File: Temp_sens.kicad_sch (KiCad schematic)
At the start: 16 parts, among them J3001 PT_1000, Q3001 IRLML5103, U3001 ADA4807-1

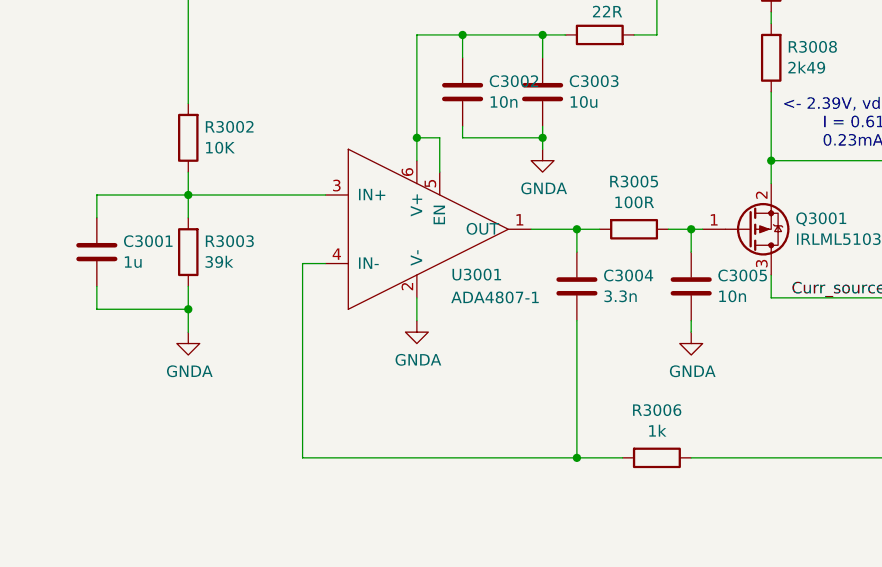
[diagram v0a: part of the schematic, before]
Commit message: added second AMUX and housekeeping
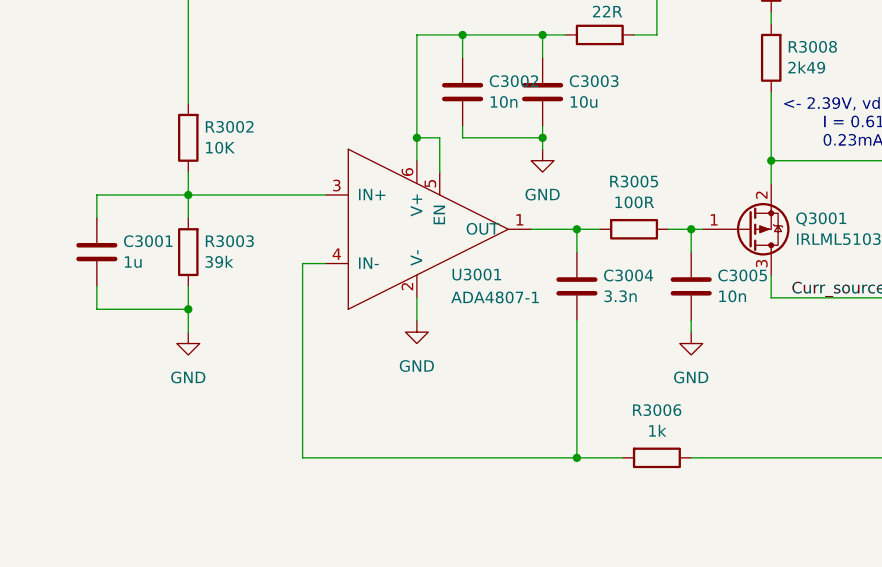
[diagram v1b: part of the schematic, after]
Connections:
- net GNDA is gone; now on net GND: C3001.2, C3002.2, C3003.2, C3005.2, R3003.1, U3001.2 (V-)

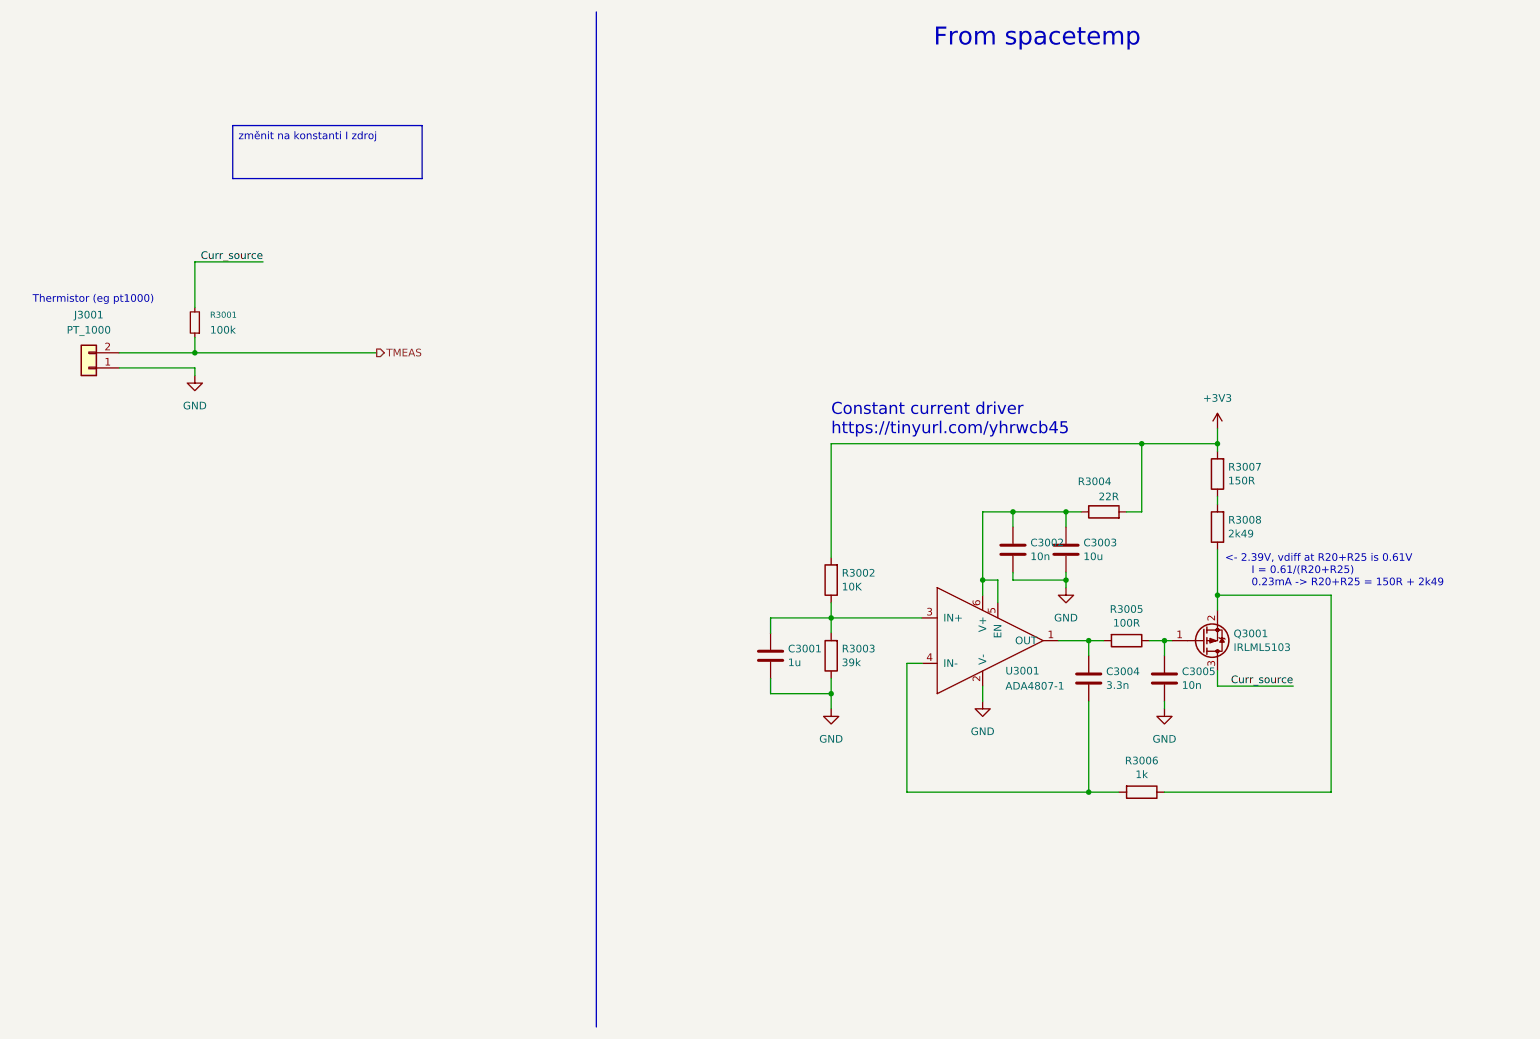
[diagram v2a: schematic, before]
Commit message: updated battery pack module; updated solar inputs module
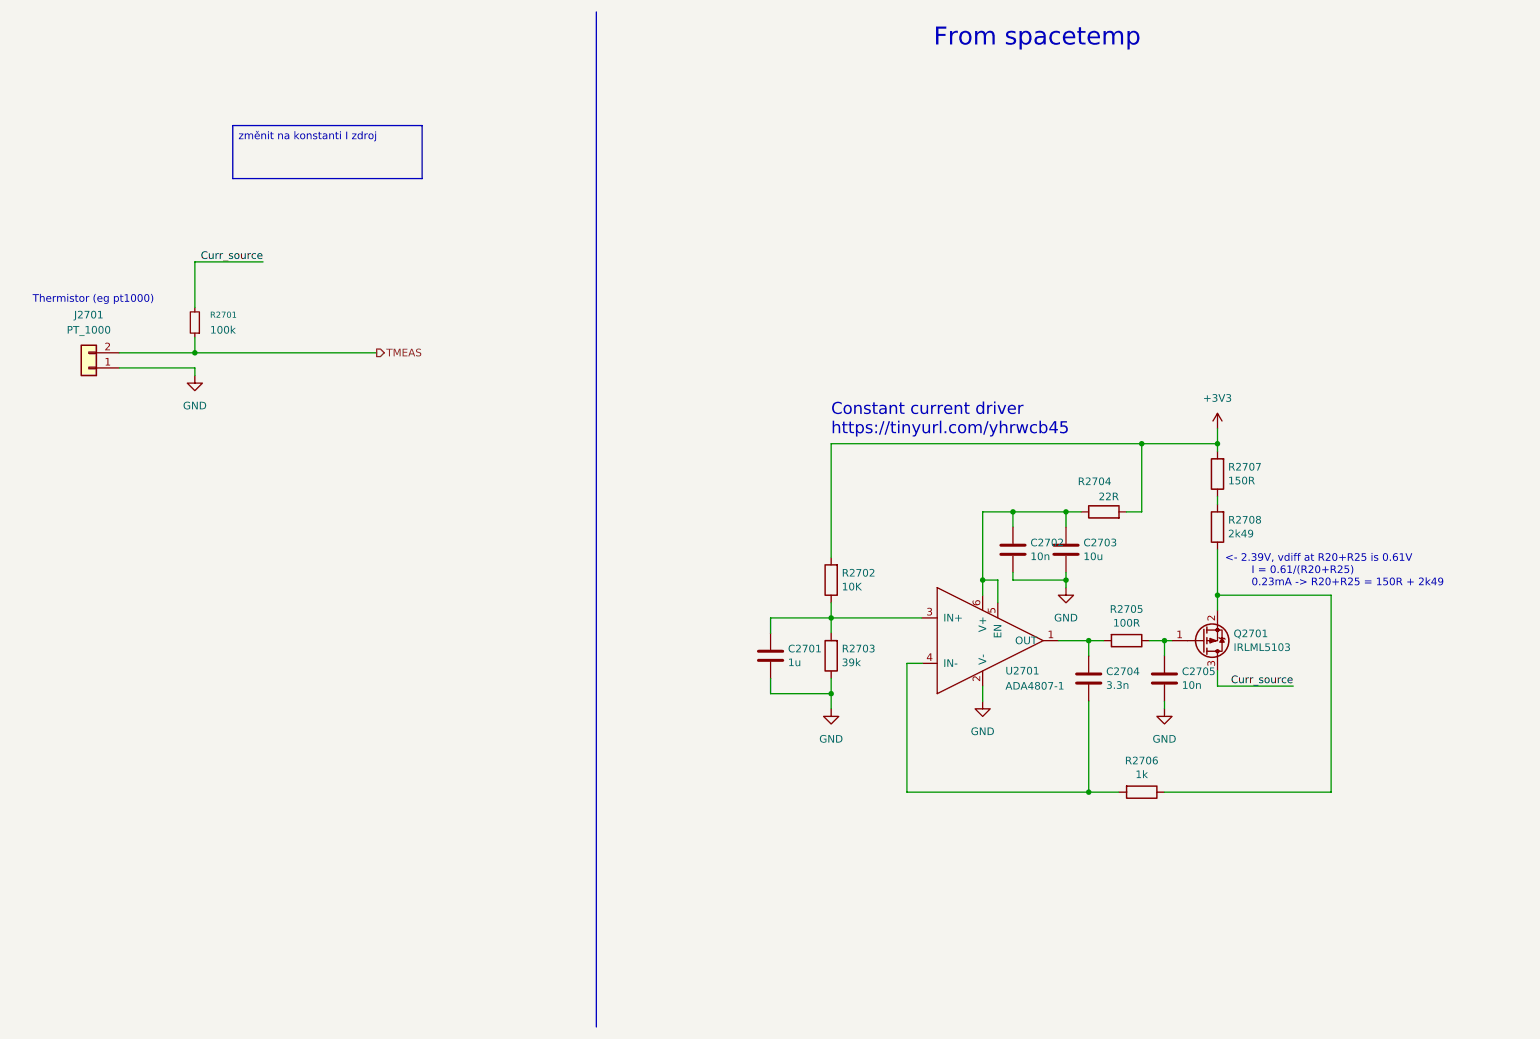
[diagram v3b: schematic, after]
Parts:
- renumbered C3001 to C2701, C3002 to C2702, C3003 to C2703, C3004 to C2704, C3005 to C2705, J3001 to J2701, Q3001 to Q2701, R3001 to R2701, R3002 to R2702, R3003 to R2703, R3004 to R2704, R3005 to R2705, R3006 to R2706, R3007 to R2707, R3008 to R2708, U3001 to U2701

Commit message: wired channel alerts; added schematic for test pbc
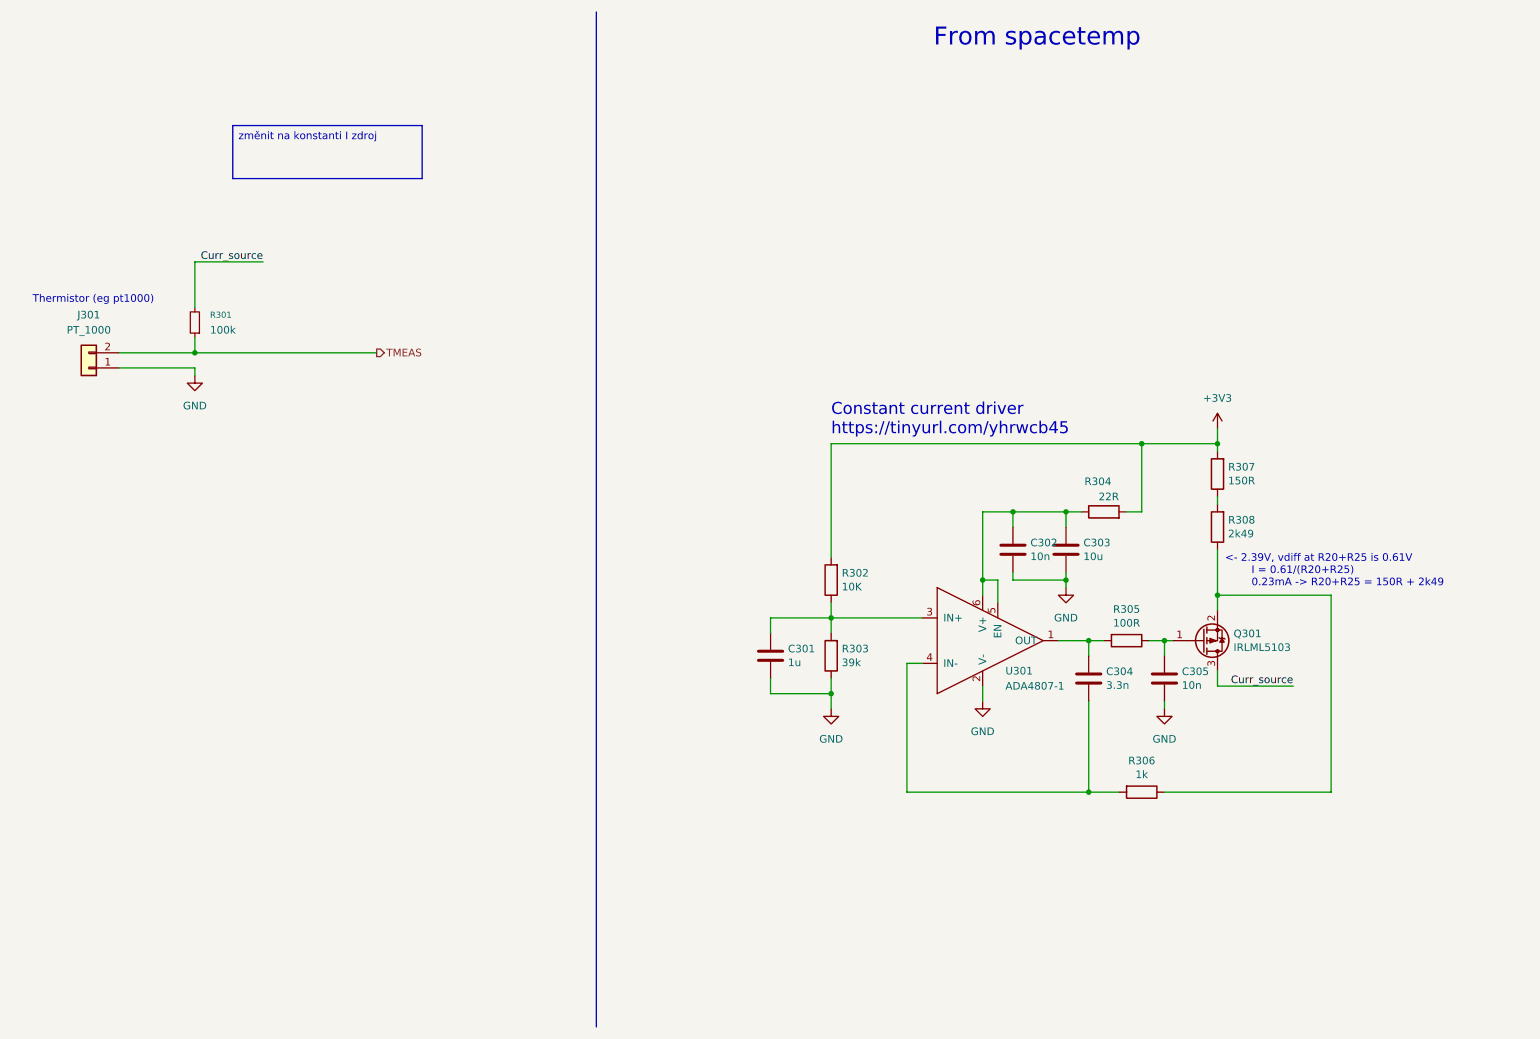
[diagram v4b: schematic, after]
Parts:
- renumbered C2701 to C301, C2702 to C302, C2703 to C303, C2704 to C304, C2705 to C305, J2701 to J301, Q2701 to Q301, R2701 to R301, R2702 to R302, R2703 to R303, R2704 to R304, R2705 to R305, R2706 to R306, R2707 to R307, R2708 to R308, U2701 to U301

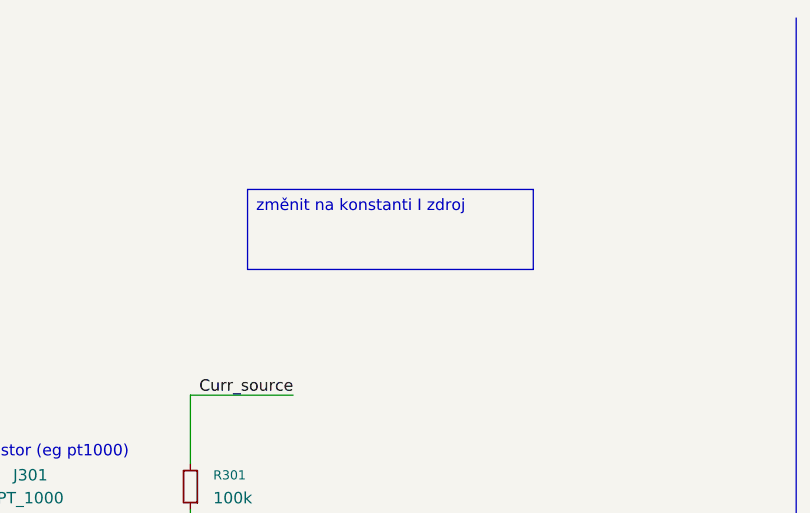
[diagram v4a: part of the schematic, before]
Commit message: reduced number of DCDC converter for PV panels; updated test pcb
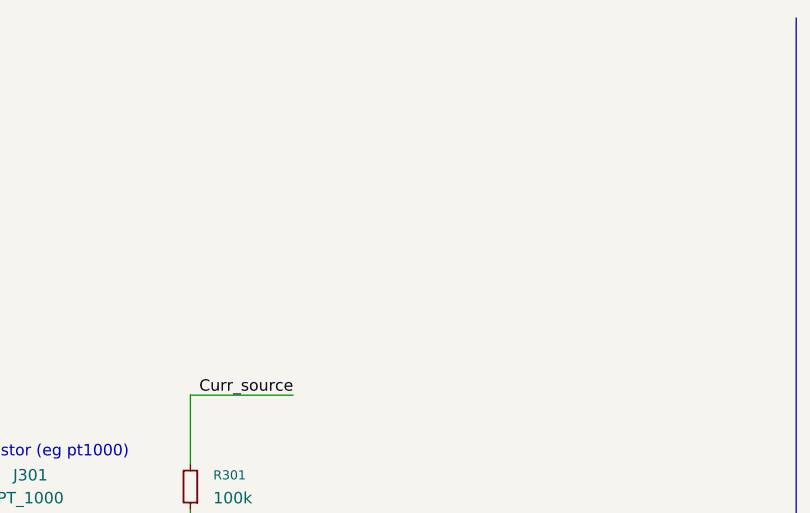
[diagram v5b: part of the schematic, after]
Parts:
- J301: footprint (none) -> Connector_PinSocket_2.54mm:PinSocket_1x02_P2.54mm_Vertical
